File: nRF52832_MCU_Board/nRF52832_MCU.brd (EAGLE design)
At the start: 55.7 x 22.9 mm, 55 parts, among them J1 HEADER_3X1, J2 HEADER_16X1, J3 HEADER_16X1, J4 HEADER_3X1, J5 MICROUSB, J6 DEBUG_CONNECTOR, J7 FPC_05P-RA-SMD, J8 MM8130-2600, U1 NRF52832, U2 TLV1117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

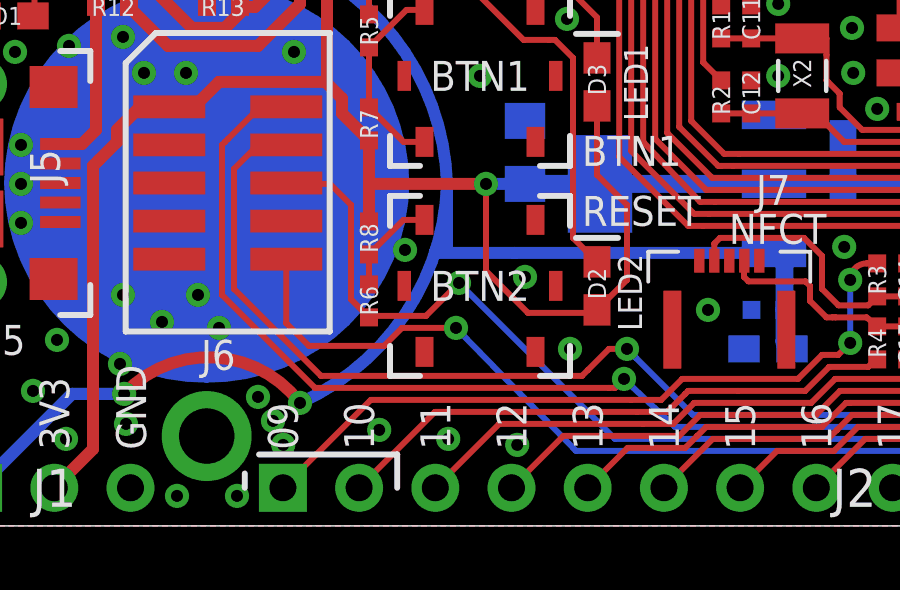
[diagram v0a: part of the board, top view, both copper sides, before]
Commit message: Issue #3: Fixed wrong connections on P0.21/RESET - 6 and P0.18/SWO - 10
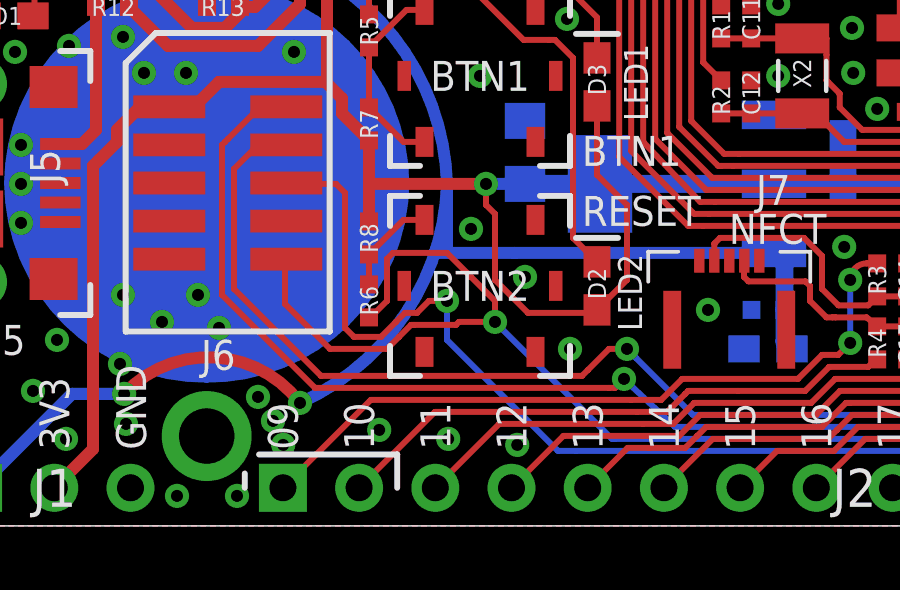
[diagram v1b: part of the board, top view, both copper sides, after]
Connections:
- net P0.18/SWO: now also J6.6; no longer J6.10
- net P0.21/RESET: now also J6.10; no longer J6.6
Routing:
- net P0.21/RESET: track 44.2 -> 49.5 mm
- net P0.18/SWO: track 36.5 -> 40.2 mm
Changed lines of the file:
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@@
 <via x="4.2" y="2.9" extent="1-16" drill="0.4" diameter="0.8"/>
 <via x="6.2" y="3.4" extent="1-16" drill="0.4" diameter="0.8"/>
-<via x="15.5" y="9.2" extent="1-16" drill="0.4" diameter="0.8"/>
+<via x="17.7" y="9.9" extent="1-16" drill="0.4" diameter="0.8"/>
 <via x="19.5" y="8.3" extent="1-16" drill="0.4" diameter="0.8"/>
 <via x="21" y="5.9" extent="1-16" drill="0.4" diameter="0.8"/>
@@
 <via x="10.6" y="4.3" extent="1-16" drill="0.4" diameter="0.8"/>
 <via x="11.1" y="3.5" extent="1-16" drill="0.4" diameter="0.8"/>
+<wire x1="15.475" y1="8" x2="17.7" y2="9.9" width="0" layer="19" extent="1-1"/>
 </signal>
 <signal name="DEC1">
@@
 <signal name="P0.18/SWO">
 <contactref element="U1" pad="21"/>
-<contactref element="J6" pad="10"/>
 <wire x1="38.34" y1="8.4" x2="38.34" y2="5.32" width="0.2" layer="1"/>
 <wire x1="33.06" y1="2.5" x2="29.5" y2="2.5" width="0.2" layer="16"/>
 <wire x1="29.5" y1="2.5" x2="21.2" y2="2.5" width="0.2" layer="16"/>
-<wire x1="21.2" y1="2.5" x2="17.2" y2="6.6" width="0.2" layer="16"/>
-<wire x1="11.54" y1="8.89" x2="11.54" y2="6.76" width="0.2" layer="1"/>
-<wire x1="11.54" y1="6.76" x2="12.3" y2="6" width="0.2" layer="1"/>
-<wire x1="12.3" y1="6" x2="14.8" y2="6" width="0.2" layer="1"/>
-<wire x1="14.8" y1="6" x2="15.4" y2="6.6" width="0.2" layer="1"/>
-<wire x1="15.4" y1="6.6" x2="17.2" y2="6.6" width="0.2" layer="1"/>
-<via x="17.2" y="6.6" extent="1-16" drill="0.4"/>
+<via x="16.9" y="7.5" extent="1-16" drill="0.4"/>
 <contactref element="J2" pad="P$10"/>
 <wire x1="34.29" y1="1.27" x2="33.06" y2="2.5" width="0.2" layer="16"/>
 <wire x1="34.29" y1="1.27" x2="38.34" y2="5.32" width="0.2" layer="1"/>
+<contactref element="J6" pad="6"/>
+<wire x1="21.2" y1="2.5" x2="20.6" y2="2.5" width="0.2" layer="16"/>
+<wire x1="20.6" y1="2.5" x2="16.9" y2="6.2" width="0.2" layer="16"/>
+<wire x1="16.9" y1="6.2" x2="16.9" y2="7.5" width="0.2" layer="16"/>
+<wire x1="16.9" y1="7.5" x2="16.3" y2="7.5" width="0.2" layer="1"/>
+<wire x1="16.3" y1="7.5" x2="15.9" y2="7.1" width="0.2" layer="1"/>
+<wire x1="15.9" y1="7.1" x2="15.5" y2="7.1" width="0.2" layer="1"/>
+<wire x1="15.5" y1="7.1" x2="15.2" y2="6.8" width="0.2" layer="1"/>
+<wire x1="15.2" y1="6.8" x2="14.7" y2="6.3" width="0.2" layer="1"/>
+<wire x1="14.7" y1="6.3" x2="13.8" y2="6.3" width="0.2" layer="1"/>
+<wire x1="13.8" y1="6.3" x2="13.5" y2="6.6" width="0.2" layer="1"/>
+<wire x1="13.5" y1="6.6" x2="13.5" y2="10.5" width="0.2" layer="1"/>
+<wire x1="13.5" y1="10.5" x2="13.5" y2="11.1" width="0.2" layer="1"/>
+<wire x1="13.5" y1="11.1" x2="13.2" y2="11.4" width="0.2" layer="1"/>
+<wire x1="13.2" y1="11.4" x2="11.57" y2="11.4" width="0.2" layer="1"/>
+<wire x1="11.57" y1="11.4" x2="11.54" y2="11.43" width="0.2" layer="1"/>
 </signal>
 <signal name="P0.19">
@@
 <signal name="P0.21/RESET">
 <contactref element="U1" pad="24"/>
-<contactref element="J6" pad="6"/>
 <wire x1="39.54" y1="8.4" x2="39.54" y2="3.64" width="0.2" layer="1"/>
 <contactref element="R6" pad="1"/>
-<wire x1="11.54" y1="11.43" x2="11.57" y2="11.4" width="0.2" layer="1"/>
-<wire x1="11.57" y1="11.4" x2="12.6" y2="11.4" width="0.2" layer="1"/>
-<wire x1="12.6" y1="11.4" x2="13" y2="11.4" width="0.2" layer="1"/>
-<wire x1="13" y1="11.4" x2="13.7" y2="10.7" width="0.2" layer="1"/>
-<wire x1="13.7" y1="10.7" x2="13.7" y2="8.6" width="0.2" layer="1"/>
-<wire x1="13.7" y1="8.6" x2="13.7" y2="7.55" width="0.2" layer="1"/>
-<wire x1="13.7" y1="7.55" x2="14.3" y2="6.95" width="0.2" layer="1"/>
-<wire x1="14.4" y1="7" x2="16.2" y2="7" width="0.2" layer="1"/>
-<wire x1="16.2" y1="7" x2="17.3" y2="8.1" width="0.2" layer="1"/>
-<wire x1="17.3" y1="8.1" x2="22.5" y2="2.9" width="0.2" layer="16"/>
 <wire x1="22.5" y1="2.9" x2="28.6" y2="2.9" width="0.2" layer="16"/>
 <wire x1="28.6" y1="2.9" x2="37.2" y2="2.9" width="0.2" layer="16"/>
-<via x="17.3" y="8.1" extent="1-16" drill="0.4"/>
+<via x="18.5" y="6.8" extent="1-16" drill="0.4"/>
 <wire x1="14.4" y1="7" x2="14.3" y2="7" width="0.2" layer="1"/>
 <wire x1="14.3" y1="7" x2="14.3" y2="6.95" width="0.2" layer="1"/>
@@
 <wire x1="39.58" y1="3.6" x2="40.3" y2="2.9" width="0.2" layer="1"/>
 <via x="40.3" y="2.9" extent="1-16" drill="0.4" diameter="0.8"/>
+<contactref element="J6" pad="10"/>
+<wire x1="22.5" y1="2.9" x2="22.4" y2="2.9" width="0.2" layer="16"/>
+<wire x1="22.4" y1="2.9" x2="18.5" y2="6.8" width="0.2" layer="16"/>
+<wire x1="18.5" y1="6.8" x2="17.3" y2="6.8" width="0.2" layer="1"/>
+<wire x1="17.3" y1="6.8" x2="17.2" y2="6.7" width="0.2" layer="1"/>
+<wire x1="17.2" y1="6.7" x2="15.8" y2="6.7" width="0.2" layer="1"/>
+<wire x1="15.8" y1="6.7" x2="15.7" y2="6.7" width="0.2" layer="1"/>
+<wire x1="15.7" y1="6.7" x2="15.3" y2="6.3" width="0.2" layer="1"/>
+<wire x1="15.3" y1="6.3" x2="14.9" y2="5.9" width="0.2" layer="1"/>
+<wire x1="14.9" y1="5.9" x2="14.2" y2="5.9" width="0.2" layer="1"/>
+<wire x1="14.2" y1="5.9" x2="13" y2="5.9" width="0.2" layer="1"/>
+<wire x1="13" y1="5.9" x2="11.5" y2="7.4" width="0.2" layer="1"/>
+<wire x1="11.5" y1="7.4" x2="11.5" y2="8.85" width="0.2" layer="1"/>
+<wire x1="11.5" y1="8.85" x2="11.54" y2="8.89" width="0.2" layer="1"/>
+<wire x1="14.3" y1="6.95" x2="14.35" y2="6.95" width="0.2" layer="1"/>
+<wire x1="14.35" y1="6.95" x2="14.9" y2="7.5" width="0.2" layer="1"/>
+<wire x1="14.9" y1="7.5" x2="14.9" y2="8.3" width="0.2" layer="1"/>
+<wire x1="14.9" y1="8.3" x2="14.9" y2="8.9" width="0.2" layer="1"/>
+<wire x1="14.9" y1="8.9" x2="15.1" y2="9.1" width="0.2" layer="1"/>
+<wire x1="15.1" y1="9.1" x2="16.6" y2="9.1" width="0.2" layer="1"/>
+<wire x1="17.7" y1="8.3" x2="18.5" y2="7.5" width="0.2" layer="1"/>
+<wire x1="18.5" y1="7.5" x2="18.5" y2="6.8" width="0.2" layer="1"/>
+<wire x1="16.6" y1="9.1" x2="16.9" y2="9.1" width="0.2" layer="1"/>
+<wire x1="16.9" y1="9.1" x2="17.7" y2="8.3" width="0.2" layer="1"/>
 </signal>
 <signal name="N$1">
@@
 <via x="18.2" y="11.4" extent="1-16" drill="0.4"/>
 <wire x1="18.2" y1="11.4" x2="19.5" y2="11.4" width="0.4" layer="16"/>
-<wire x1="18.2" y1="11.4" x2="18.2" y2="8.5" width="0.2" layer="1"/>
-<wire x1="18.2" y1="8.5" x2="19.6" y2="7.1" width="0.2" layer="1"/>
+<wire x1="18.5" y1="8.2" x2="19.6" y2="7.1" width="0.2" layer="1"/>
 <wire x1="19.6" y1="7.1" x2="21.8" y2="7.1" width="0.2" layer="1"/>
 <wire x1="21.8" y1="7.1" x2="21.9" y2="7.2" width="0.2" layer="1"/>
@@
 <wire x1="3.81" y1="21.59" x2="3.81" y2="21.19" width="0.4064" layer="1"/>
 <wire x1="34.04" y1="14.4" x2="34.4" y2="14.4" width="0.2" layer="1"/>
+<wire x1="18.2" y1="11.4" x2="18.2" y2="10.7" width="0.2" layer="1"/>
+<wire x1="18.2" y1="10.7" x2="18.5" y2="10.4" width="0.2" layer="1"/>
+<wire x1="18.5" y1="10.4" x2="18.5" y2="9" width="0.2" layer="1"/>
+<wire x1="18.5" y1="9" x2="18.5" y2="8.2" width="0.2" layer="1"/>
 </signal>
 <signal name="N$8">
